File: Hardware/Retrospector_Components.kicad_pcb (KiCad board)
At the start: 4 copper layers, 60 x 110 mm, 145 parts, among them J1 SWD_Header, J2 Eurorack_10_pin_power, J3 Conn_01x08_Male, J4 Conn_01x08_Male, J5 Conn_01x08_Male, J6 Conn_01x08_Male, J7 USB_B_Micro, U1 STM32H743ZITx, U10 LM2675M-5, U11 TL072, U2 IS42S16800F-7TLI, U3 PCM5100APW, U4 SSI2164, U5 MCP6004, U6 MCP6004, U7 TL074, U8 LD1117-3.3-4Tab, Y1 8MHz 20pF

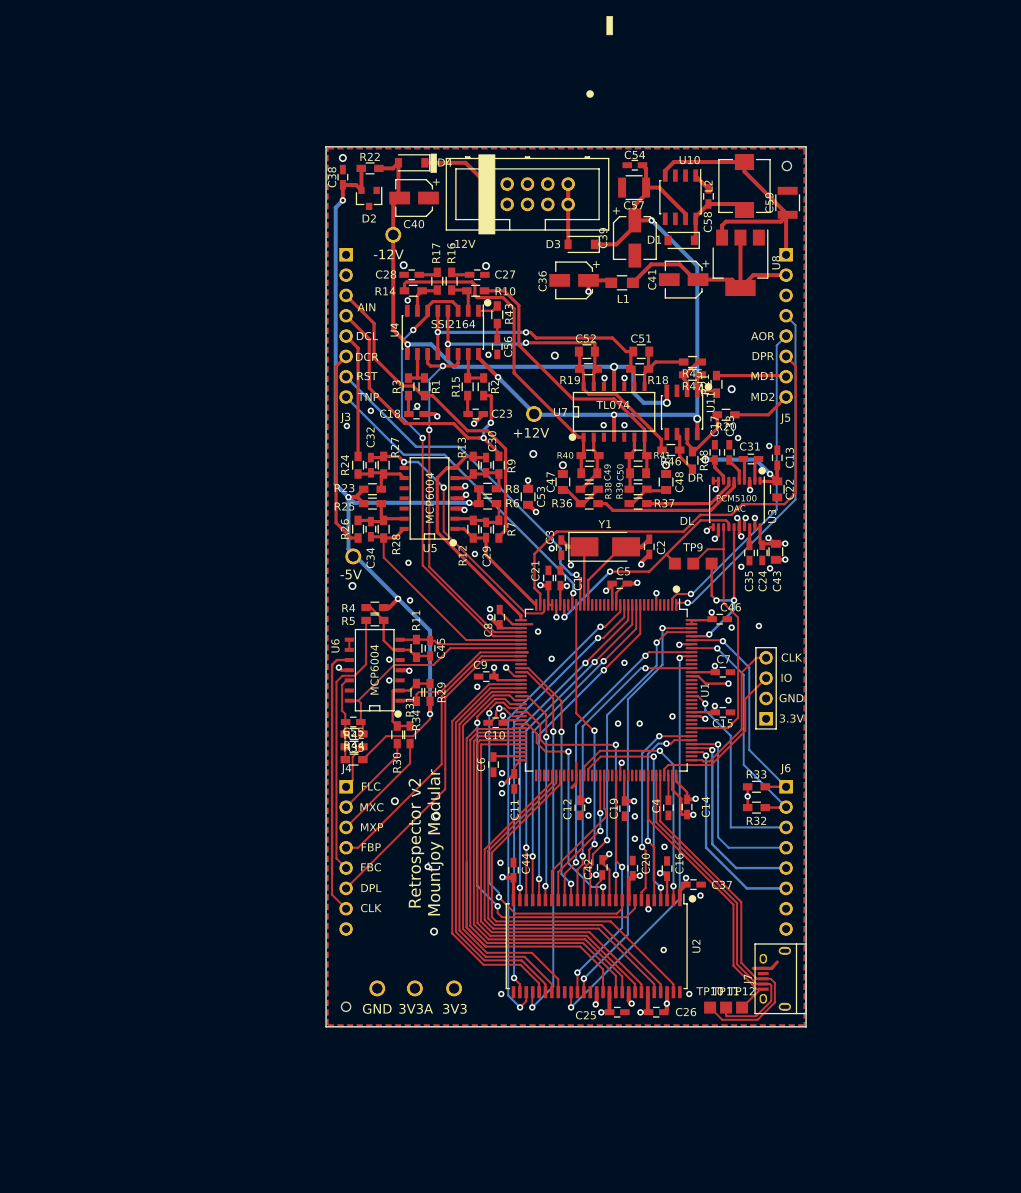
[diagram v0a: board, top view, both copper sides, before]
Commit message: Added some test code using SPI to control Toshiba LED controller
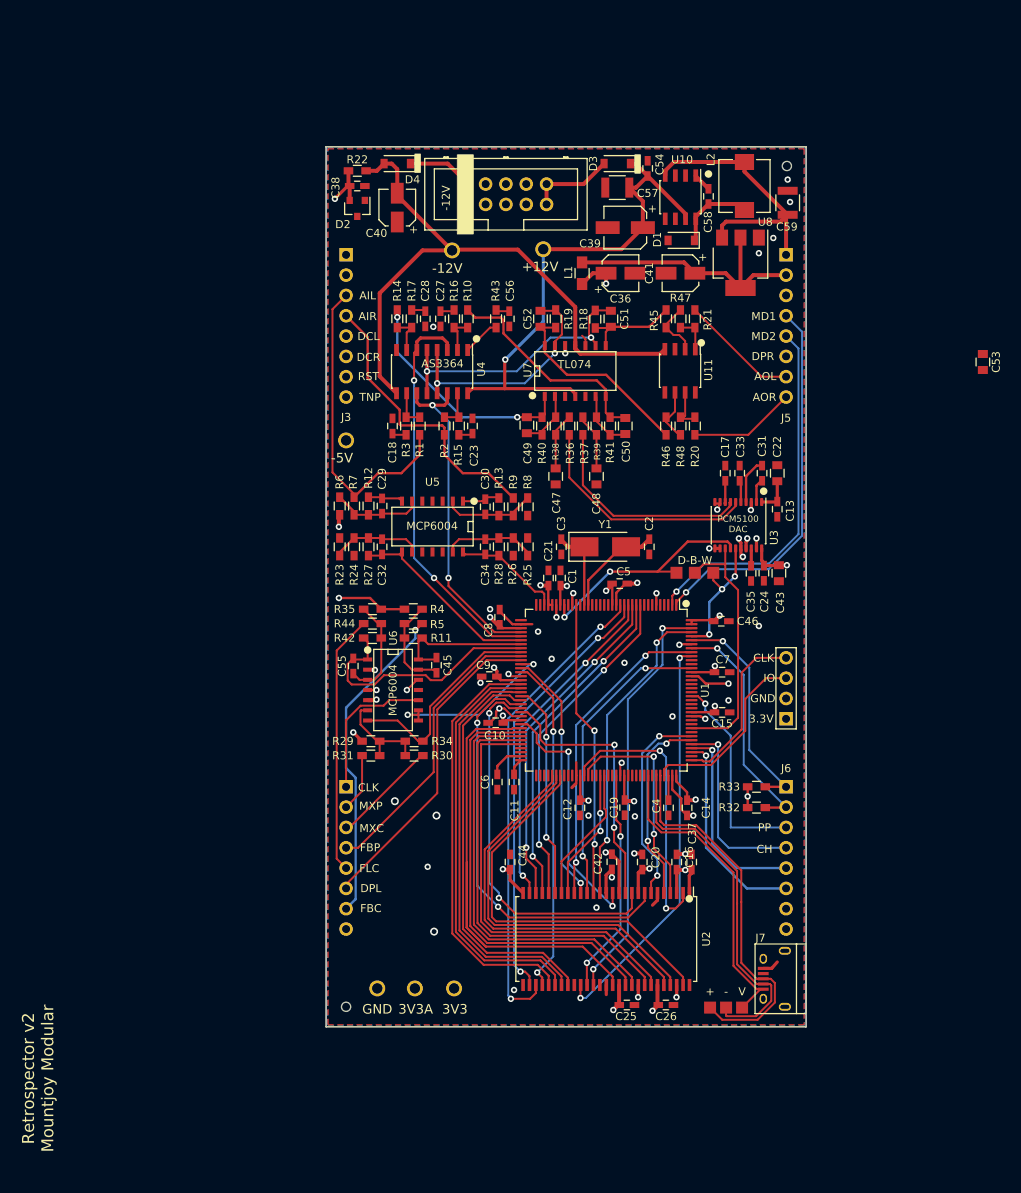
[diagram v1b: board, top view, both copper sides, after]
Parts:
- U4: value SSI2164 -> AS3364
- moved C53 59.3 mm to (182.1, 76.9)
- moved TP5 20.6 mm to (127.2, 62.8)
- moved R25 20.1 mm to (125.2, 100.0), turned to 90 degrees
- moved R26 19.5 mm to (123.4, 100.0)
- moved R35 18.9 mm to (105.8, 107.8)
- moved R6 18.5 mm to (101.7, 94.9), turned to 270 degrees
- moved R7 18.3 mm to (103.5, 94.9), turned to 90 degrees
- moved R42 15.6 mm to (105.8, 109.6), turned to 180 degrees
- moved R28 14.6 mm to (121.6, 100.0)
- moved TP4 14.5 mm to (102.5, 86.7)
- moved C34 14.5 mm to (119.9, 100.0)
- moved R12 13.4 mm to (105.3, 94.9), turned to 270 degrees
- moved C29 13.3 mm to (107.0, 94.9), turned to 270 degrees
- moved R44 12.2 mm to (105.8, 111.4), turned to 0 degrees
- moved R37 11.9 mm to (132.1, 84.9), turned to 270 degrees
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- renumbered TP10 to +, TP11 to -, TP9 to D-B-W, TP12 to V
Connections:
- J4 pad 1: /FILTER_CV -> /CLOCK
- J4 pad 2: /MIX_CV -> /MIX_POT
- J4 pad 3: /MIX_POT -> /MIX_CV
- J4 pad 5: /FEEDBACK_CV -> /FILTER_CV
- J4 pad 7: /CLOCK -> /FEEDBACK_CV
- U1 pad 127: /CLOCK_SCALED -> Net-(U1-Pad127)
- U1 pad 34: /DELAY_CV_SCALED_L -> /DELAY_CV_SCALED_R
- U1 pad 42: /DELAY_CV_SCALED_R -> /DELAY_CV_SCALED_L
- U1 pad 48: Net-(U1-Pad48) -> /CLOCK_SCALED
- U5 pad 1: /AUDIO_IN_L -> /AUDIO_IN_R
- U5 pad 2: Net-(C29-Pad2) -> Net-(C30-Pad2)
- U5 pad 6: Net-(C30-Pad2) -> Net-(C29-Pad2)
- U5 pad 7: /AUDIO_IN_R -> /AUDIO_IN_L
- U6 pad 1: /WET_DRY_MIX -> /FILTER_CV_SCALED
- U6 pad 12: Net-(C55-Pad2) -> GND
- U6 pad 13: GND -> Net-(C45-Pad2)
- U6 pad 14: /FILTER_CV_SCALED -> /FEEDBACK_CV_SCALED
- U6 pad 2: Net-(R29-Pad1) -> GND
- U6 pad 3: GND -> Net-(C55-Pad2)
- U6 pad 6: Net-(C45-Pad2) -> Net-(R29-Pad1)
- U6 pad 7: /FEEDBACK_CV_SCALED -> /WET_DRY_MIX
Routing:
- net /DELAY_POT_R: track 60.2 -> 0.00 mm
- net /RESET: track 44.1 -> 0.00 mm, vias 1 -> 0
- net /TONE_POT: track 40.8 -> 1.51 mm
- net /FILTER_CV: track 5.87 -> 32.7 mm
- net /-5V_REF: track 114.7 -> 88.2 mm, vias 5 -> 4
- net /DELAY_CV_R: track 24.9 -> 0.00 mm
- net /AUDIO_IN_R: track 29.3 -> 4.70 mm
- net /CLOCK_SCALED: track 1.27 -> 22.5 mm, vias 0 -> 2
- net VCC: track 86.3 -> 66.0 mm, vias 4 -> 1
- net /DELAY_CV_L: track 15.7 -> 0.00 mm
- net /CLOCK: track 33.6 -> 18.4 mm
- net /DELAY_CV_SCALED_R: track 28.9 -> 13.7 mm
- net +3.3VA: track 30.5 -> 16.9 mm, vias 7 -> 3
- net /DAC_OUT_AMP_L: track 41.5 -> 29.3 mm, vias 0 -> 2
- net GND: track 79.6 -> 68.5 mm, vias 84 -> 45
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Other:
- board text added: "AIL"
- board text added: "AIR"
- board text added: "AOL"
- board text added: "CH"
- board text added: "PP"
- board text removed: "AIN"
- board text removed: "DL"
- board text removed: "DR"
- board text removed: "J4"

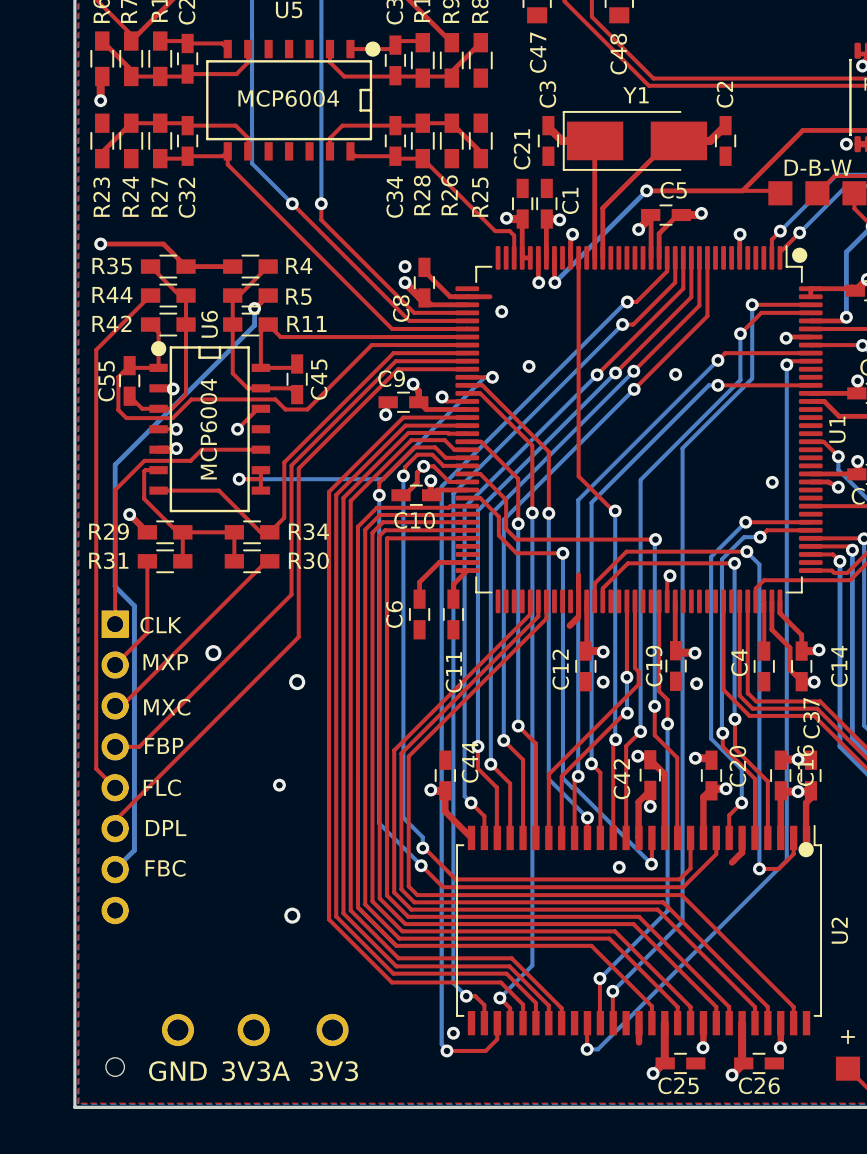
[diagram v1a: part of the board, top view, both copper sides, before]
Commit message: Basic tests of Toshiba LED Driver using SPI
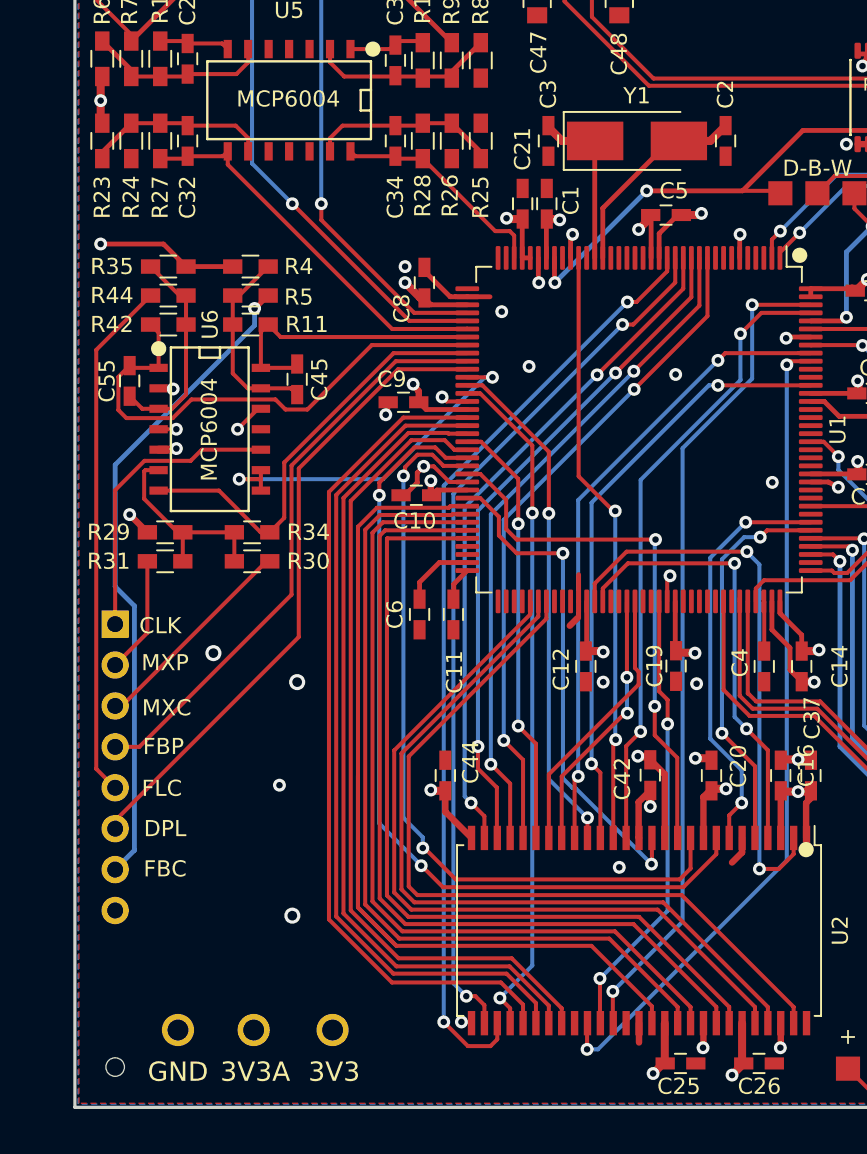
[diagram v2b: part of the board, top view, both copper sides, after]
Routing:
- net /-5V_REF: track 88.2 -> 89.6 mm
- net /FMC_A5: track 60.0 -> 58.6 mm
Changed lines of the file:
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@@
     (thickness 1.6)
     (drawings 46)
-    (tracks 1215)
+    (tracks 1212)
     (zones 0)
     (modules 145)
@@
   (via (at 128.2 114) (size 0.8) (drill 0.4) (layers F.Cu B.Cu) (net 1))
   (via (at 137.3 114.5) (size 0.8) (drill 0.4) (layers F.Cu B.Cu) (net 1))
-  (via (at 123.5 155.4) (size 0.8) (drill 0.4) (layers F.Cu B.Cu) (net 1))
+  (via (at 124 154.7) (size 0.8) (drill 0.4) (layers F.Cu B.Cu) (net 1))
   (segment (start 121.65529 120.204324) (end 121.255291 120.604323) (width 0.3) (layer F.Cu) (net 1))
   (segment (start 121.255291 120.604323) (end 121.255291 121.219709) (width 0.3) (layer F.Cu) (net 1))
@@
   (via (at 132.075 138.675) (size 0.8) (drill 0.4) (layers F.Cu B.Cu) (net 82))
   (via (at 139.925 115.175) (size 0.8) (drill 0.4) (layers F.Cu B.Cu) (net 82))
-  (segment (start 141.4 141.1) (end 141.4 139.017311) (width 0.25) (layer B.Cu) (net 90))
-  (segment (start 141.4 139.017311) (end 139.499999 137.11731) (width 0.25) (layer B.Cu) (net 90))
-  (segment (start 139.499999 137.11731) (end 139.499999 125.825001) (width 0.25) (layer B.Cu) (net 90))
   (segment (start 140.625 143.275) (end 140.625 141.875) (width 0.25) (layer F.Cu) (net 90) (status 10))
   (segment (start 140.625 141.875) (end 141.4 141.1) (width 0.25) (layer F.Cu) (net 90))
   (via (at 141.4 141.1) (size 0.8) (drill 0.4) (layers F.Cu B.Cu) (net 90))
-  (segment (start 139.499999 125.825001) (end 141.65 123.675) (width 0.25) (layer B.Cu) (net 90))
   (segment (start 141.65 123.675) (end 145.6875 123.675) (width 0.25) (layer F.Cu) (net 90) (status 20))
   (via (at 141.65 123.675) (size 0.8) (drill 0.4) (layers F.Cu B.Cu) (net 90))
+  (segment (start 141.4 141.1) (end 141.4 139.06911) (width 0.25) (layer B.Cu) (net 90))
+  (segment (start 141.4 139.06911) (end 139.44895 137.11806) (width 0.25) (layer B.Cu) (net 90))
+  (segment (start 139.44895 137.11806) (end 139.44895 125.87605) (width 0.25) (layer B.Cu) (net 90))
+  (segment (start 139.44895 125.87605) (end 141.65 123.675) (width 0.25) (layer B.Cu) (net 90))
   (segment (start 142.55 124.6) (end 142.975 124.175) (width 0.25) (layer F.Cu) (net 91))
   (segment (start 142.975 124.175) (end 144.95 124.175) (width 0.25) (layer F.Cu) (net 91) (status 20))
   (segment (start 144.95 124.175) (end 145.6875 124.175) (width 0.25) (layer F.Cu) (net 91) (status 30))
-  (segment (start 140.225 137.607824) (end 140.225 136.769309) (width 0.25) (layer F.Cu) (net 91))
-  (segment (start 142.225 143.275) (end 142.225 139.607824) (width 0.25) (layer F.Cu) (net 91) (status 10))
-  (segment (start 142.225 139.607824) (end 140.225 137.607824) (width 0.25) (layer F.Cu) (net 91))
-  (segment (start 140.174999 125.976999) (end 141.551998 124.6) (width 0.25) (layer B.Cu) (net 91))
-  (segment (start 140.225 136.769309) (end 140.174999 136.719308) (width 0.25) (layer B.Cu) (net 91))
-  (segment (start 140.174999 136.719308) (end 140.174999 125.976999) (width 0.25) (layer B.Cu) (net 91))
-  (segment (start 141.551998 124.6) (end 142.55 124.6) (width 0.25) (layer B.Cu) (net 91))
   (via (at 142.55 124.6) (size 0.8) (drill 0.4) (layers F.Cu B.Cu) (net 91))
-  (via (at 140.225 136.769309) (size 0.8) (drill 0.4) (layers F.Cu B.Cu) (net 91))
+  (via (at 140.173952 136.770058) (size 0.8) (drill 0.4) (layers F.Cu B.Cu) (net 91))
+  (segment (start 142.225 143.275) (end 142.225 138.821106) (width 0.25) (layer F.Cu) (net 91))
+  (segment (start 142.225 138.821106) (end 140.173952 136.770058) (width 0.25) (layer F.Cu) (net 91))
+  (segment (start 142.55 124.6) (end 141.551998 124.6) (width 0.25) (layer B.Cu) (net 91))
+  (segment (start 141.551998 124.6) (end 140.173952 125.978046) (width 0.25) (layer B.Cu) (net 91))
+  (segment (start 140.173952 125.978046) (end 140.173952 136.770058) (width 0.25) (layer B.Cu) (net 91))
   (segment (start 132.6 152) (end 132.6 154.75) (width 0.25) (layer F.Cu) (net 97) (status 20))
   (segment (start 132.6 154.75) (end 132.625 154.775) (width 0.25) (layer F.Cu) (net 97) (status 30))
@@
   (segment (start 134.151998 135.525) (end 130.225 139.451998) (width 0.25) (layer F.Cu) (net 101))
   (segment (start 130.225 139.451998) (end 130.225 143.275) (width 0.25) (layer F.Cu) (net 101) (status 20))
-  (segment (start 140.984849 137.731262) (end 140.984849 135.900002) (width 0.25) (layer F.Cu) (net 104))
-  (segment (start 143.025 143.275) (end 143.025 139.771413) (width 0.25) (layer F.Cu) (net 104) (status 10))
-  (segment (start 143.025 139.771413) (end 140.984849 137.731262) (width 0.25) (layer F.Cu) (net 104))
-  (segment (start 140.956778 126.225) (end 140.956778 135.871931) (width 0.25) (layer B.Cu) (net 104))
-  (segment (start 140.956778 135.871931) (end 140.984849 135.900002) (width 0.25) (layer B.Cu) (net 104))
-  (via (at 140.984849 135.900002) (size 0.8) (drill 0.4) (layers F.Cu B.Cu) (net 104))
   (segment (start 140.956778 126.225) (end 134.334298 126.225) (width 0.25) (layer F.Cu) (net 104))
   (segment (start 134.334298 126.225) (end 132.775 127.784298) (width 0.25) (layer F.Cu) (net 104))
   (segment (start 132.775 127.784298) (end 132.775 127.85) (width 0.25) (layer F.Cu) (net 104) (status 20))
   (via (at 140.956778 126.225) (size 0.8) (drill 0.4) (layers F.Cu B.Cu) (net 104))
+  (segment (start 143.025 137.825) (end 141.7 136.5) (width 0.25) (layer F.Cu) (net 104))
+  (segment (start 140.956778 135.756778) (end 141.7 136.5) (width 0.25) (layer B.Cu) (net 104))
+  (segment (start 143.025 143.275) (end 143.025 137.825) (width 0.25) (layer F.Cu) (net 104))
+  (via (at 141.7 136.5) (size 0.8) (drill 0.4) (layers F.Cu B.Cu) (net 104))
+  (segment (start 140.956778 126.225) (end 140.956778 135.756778) (width 0.25) (layer B.Cu) (net 104))
   (via (at 142.5 145.2) (size 0.8) (drill 0.4) (layers F.Cu B.Cu) (net 105))
   (segment (start 144.625 143.275) (end 144.625 144.28) (width 0.25) (layer F.Cu) (net 105) (status 10))
@@
   (via (at 133.575 137.175) (size 0.8) (drill 0.4) (layers F.Cu B.Cu) (net 136))
   (segment (start 133.425 143.275) (end 133.425 137.325) (width 0.25) (layer F.Cu) (net 136) (status 10))
-  (segment (start 123.1 156.5) (end 123.1 156.425) (width 0.25) (layer B.Cu) (net 140))
-  (segment (start 123.1 156.425) (end 122.773001 156.098001) (width 0.25) (layer B.Cu) (net 140))
-  (segment (start 126.225 154.775) (end 126.225 155.78) (width 0.25) (layer F.Cu) (net 140) (status 10))
-  (segment (start 126.225 155.78) (end 125.505 156.5) (width 0.25) (layer F.Cu) (net 140))
-  (via (at 123.1 156.5) (size 0.8) (drill 0.4) (layers F.Cu B.Cu) (net 140))
-  (segment (start 125.505 156.5) (end 123.1 156.5) (width 0.25) (layer F.Cu) (net 140))
-  (segment (start 122.773001 156.098001) (end 122.773001 121.453995) (width 0.25) (layer B.Cu) (net 140))
-  (segment (start 134.226996 110) (end 134.3 110) (width 0.25) (layer B.Cu) (net 140))
-  (segment (start 122.773001 121.453995) (end 134.226996 110) (width 0.25) (layer B.Cu) (net 140))
   (segment (start 134.865685 110) (end 134.3 110) (width 0.25) (layer F.Cu) (net 140))
   (segment (start 136.775 108.090685) (end 134.865685 110) (width 0.25) (layer F.Cu) (net 140))
   (segment (start 136.775 107.2625) (end 136.775 108.090685) (width 0.25) (layer F.Cu) (net 140) (status 10))
   (via (at 134.3 110) (size 0.8) (drill 0.4) (layers F.Cu B.Cu) (net 140))
+  (via (at 122.9 154.700002) (size 0.8) (drill 0.4) (layers F.Cu B.Cu) (net 140))
+  (segment (start 125.805001 156.199999) (end 124.399997 156.199999) (width 0.25) (layer F.Cu) (net 140))
+  (segment (start 126.225 154.775) (end 126.225 155.78) (width 0.25) (layer F.Cu) (net 140))
+  (segment (start 126.225 155.78) (end 125.805001 156.199999) (width 0.25) (layer F.Cu) (net 140))
+  (segment (start 124.399997 156.199999) (end 122.9 154.700002) (width 0.25) (layer F.Cu) (net 140))
+  (segment (start 134.3 110) (end 122.9 121.4) (width 0.25) (layer B.Cu) (net 140))
+  (segment (start 122.9 121.4) (end 122.9 154.700002) (width 0.25) (layer B.Cu) (net 140))
   (segment (start 124.3 153.1) (end 124.865685 153.1) (width 0.25) (layer F.Cu) (net 141))
   (segment (start 124.865685 153.1) (end 125.425 153.659315) (width 0.25) (layer F.Cu) (net 141))
@@
   (segment (start 101.6 96.1) (end 101.7 96) (width 0.5) (layer F.Cu) (net 165))
   (segment (start 101.6 97.5) (end 101.6 96.1) (width 0.5) (layer F.Cu) (net 165))
+  (segment (start 101.6 98.8) (end 101.7 98.9) (width 0.5) (layer F.Cu) (net 165))
+  (segment (start 101.6 97.5) (end 101.6 98.8) (width 0.5) (layer F.Cu) (net 165))
   (segment (start 146.205 59) (end 146.205 58.745) (width 0.5) (layer F.Cu) (net 166) (status 30))
   (segment (start 146.205 58.745) (end 147.8 57.15) (width 0.5) (layer F.Cu) (net 166) (status 30))
